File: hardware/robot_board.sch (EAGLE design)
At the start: 152 parts, among them J1 POWER_JACKPTH, Q1 DMP2035U, Q2 DMP2035U, Q3 DMP2035U-7, Q4 DMP2035U-7, U1 FT232RL-BASICSSOP, U10 DRV8839, U11 LM393, U12 LM393, U16 LM393, U17 ATMEGA325PA, U2 SIA907EDJT, U3 MIC5219, U4 HC_05, U5 SIA907EDJT, U6 SIA907EDJT, U7 TLV70233, U8 MIC2009A, U9 DRV8839, Y1 16MHz

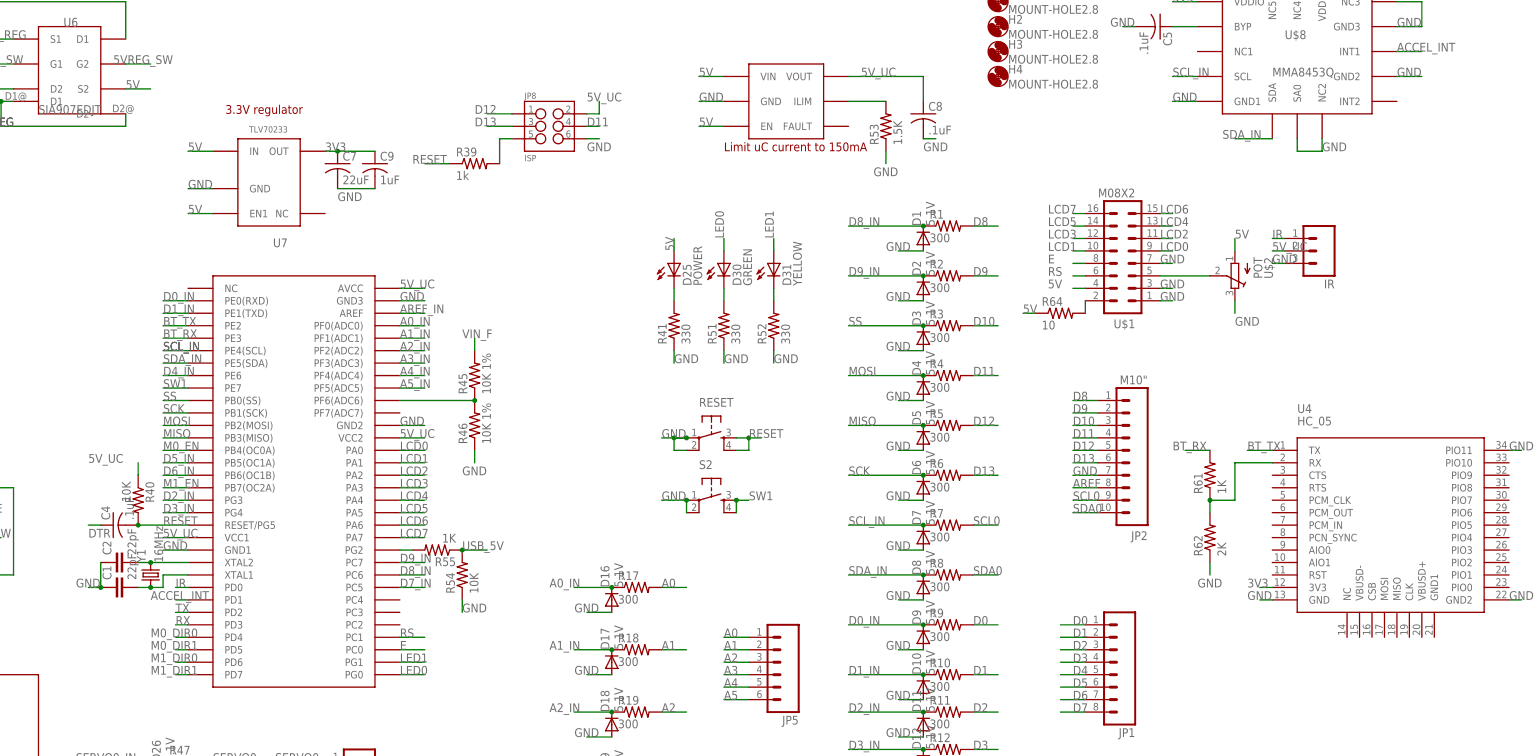
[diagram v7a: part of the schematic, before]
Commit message: fix servo bug
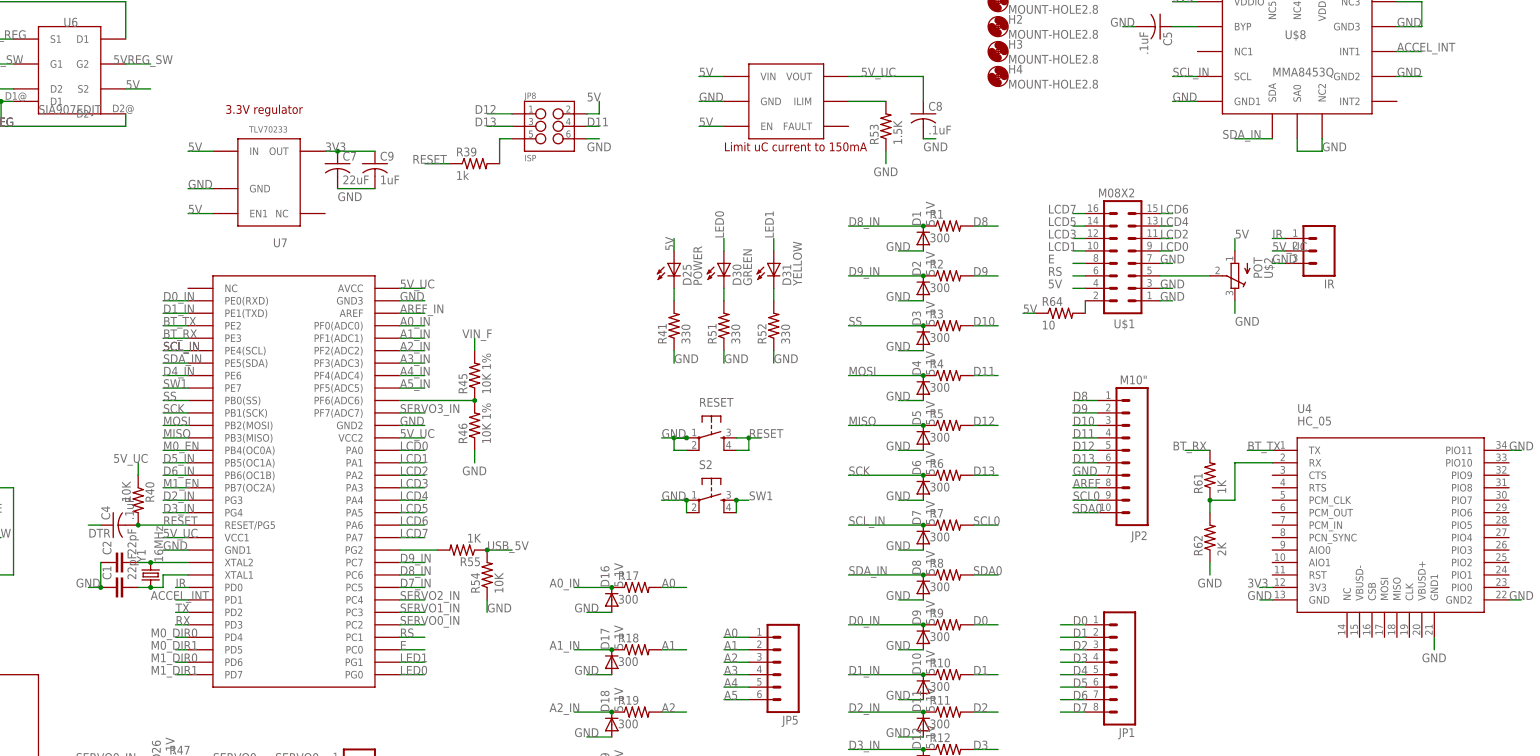
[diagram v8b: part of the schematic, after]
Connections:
- net 5V: now also JP8.2
- net 5V_UC: no longer JP8.2
- net GND: now also U4.GND1
- net SERVO0_IN: now also U17.PC2
- net SERVO1_IN: now also U17.PC3
- net SERVO2_IN: now also U17.PC4
- net SERVO3_IN: now also U17.PF7(ADC7)
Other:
- moved on the sheet: R54, R55
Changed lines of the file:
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@@
 <instance part="U8" gate="G$1" x="233.68" y="106.68"/>
 <instance part="R53" gate="G$1" x="254" y="106.68" rot="R90"/>
-<instance part="R54" gate="G$1" x="167.64" y="15.24" rot="R90"/>
-<instance part="R55" gate="G$1" x="162.56" y="20.32" rot="R180"/>
+<instance part="R54" gate="G$1" x="172.72" y="15.24" rot="R90"/>
+<instance part="R55" gate="G$1" x="167.64" y="20.32" rot="R180"/>
 <instance part="U7" gate="G$1" x="129.54" y="101.6" rot="R180"/>
 <instance part="U$8" gate="G$1" x="337.82" y="121.92"/>
@@
 <segment>
 <pinref part="R54" gate="G$1" pin="1"/>
-<wire x1="167.64" y1="10.16" x2="167.64" y2="7.62" width="0.1524" layer="91"/>
-<label x="167.64" y="7.62" size="1.778" layer="95"/>
+<wire x1="172.72" y1="10.16" x2="172.72" y2="7.62" width="0.1524" layer="91"/>
+<label x="172.72" y="7.62" size="1.778" layer="95"/>
 </segment>
 <segment>
@@
 <wire x1="325.12" y1="71.12" x2="325.12" y2="68.58" width="0.1524" layer="91"/>
 <label x="325.12" y="66.04" size="1.778" layer="95"/>
+</segment>
+<segment>
+<pinref part="U4" gate="G$1" pin="GND1"/>
+<wire x1="365.76" y1="2.54" x2="365.76" y2="0" width="0.1524" layer="91"/>
+<label x="363.22" y="-2.54" size="1.778" layer="95"/>
 </segment>
 </net>
@@
 </segment>
 <segment>
-<pinref part="JP8" gate="G$1" pin="2"/>
-<wire x1="193.04" y1="109.22" x2="195.58" y2="109.22" width="0.1524" layer="91"/>
-<wire x1="195.58" y1="109.22" x2="195.58" y2="111.76" width="0.1524" layer="91"/>
-<label x="193.04" y="111.76" size="1.778" layer="95"/>
-</segment>
-<segment>
 <pinref part="U17" gate="G$1" pin="VCC1"/>
 <wire x1="111.76" y1="22.86" x2="106.68" y2="22.86" width="0.1524" layer="91"/>
@@
 <pinref part="R40" gate="G$1" pin="1"/>
 <wire x1="101.6" y1="35.56" x2="101.6" y2="38.1" width="0.1524" layer="91"/>
-<label x="91.44" y="38.1" size="1.778" layer="95"/>
+<label x="96.52" y="38.1" size="1.778" layer="95"/>
 </segment>
 <segment>
@@
 <segment>
 <pinref part="R54" gate="G$1" pin="2"/>
-<wire x1="167.64" y1="20.32" x2="172.72" y2="20.32" width="0.1524" layer="91"/>
-<label x="167.64" y="20.32" size="1.778" layer="95"/>
+<wire x1="172.72" y1="20.32" x2="177.8" y2="20.32" width="0.1524" layer="91"/>
+<label x="172.72" y="20.32" size="1.778" layer="95"/>
 <pinref part="R55" gate="G$1" pin="1"/>
-<junction x="167.64" y="20.32"/>
+<junction x="172.72" y="20.32"/>
 </segment>
 <segment>
@@
 <label x="281.94" y="68.58" size="1.778" layer="95"/>
 </segment>
+<segment>
+<pinref part="JP8" gate="G$1" pin="2"/>
+<wire x1="193.04" y1="109.22" x2="195.58" y2="109.22" width="0.1524" layer="91"/>
+<wire x1="195.58" y1="109.22" x2="195.58" y2="111.76" width="0.1524" layer="91"/>
+<label x="193.04" y="111.76" size="1.778" layer="95"/>
+</segment>
 </net>
 <net name="N$28" class="0">
@@
 <junction x="106.68" y="-22.86"/>
 </segment>
+<segment>
+<pinref part="U17" gate="G$1" pin="PC2"/>
+<wire x1="154.94" y1="5.08" x2="160.02" y2="5.08" width="0.1524" layer="91"/>
+<label x="154.94" y="5.08" size="1.778" layer="95"/>
+</segment>
 </net>
 <net name="SERVO1_IN" class="0">
@@
 <junction x="106.68" y="-35.56"/>
 </segment>
+<segment>
+<pinref part="U17" gate="G$1" pin="PC3"/>
+<wire x1="154.94" y1="7.62" x2="160.02" y2="7.62" width="0.1524" layer="91"/>
+<label x="154.94" y="7.62" size="1.778" layer="95"/>
+</segment>
 </net>
 <net name="SERVO2_IN" class="0">
@@
 <junction x="106.68" y="-50.8"/>
 </segment>
+<segment>
+<pinref part="U17" gate="G$1" pin="PC4"/>
+<wire x1="154.94" y1="10.16" x2="160.02" y2="10.16" width="0.1524" layer="91"/>
+<label x="154.94" y="10.16" size="1.778" layer="95"/>
+</segment>
 </net>
 <net name="SERVO3_IN" class="0">
@@
 <junction x="106.68" y="-63.5"/>
 </segment>
+<segment>
+<pinref part="U17" gate="G$1" pin="PF7(ADC7)"/>
+<wire x1="154.94" y1="48.26" x2="160.02" y2="48.26" width="0.1524" layer="91"/>
+<label x="154.94" y="48.26" size="1.778" layer="95"/>
+</segment>
 </net>
 <net name="M0_EN" class="0">
@@
 <pinref part="R55" gate="G$1" pin="2"/>
 <pinref part="U17" gate="G$1" pin="PG2"/>
-<wire x1="157.48" y1="20.32" x2="154.94" y2="20.32" width="0.1524" layer="91"/>
-</segment>
-</net>
+<wire x1="162.56" y1="20.32" x2="154.94" y2="20.32" width="0.1524" layer="91"/>
+</segment>
+</net>
